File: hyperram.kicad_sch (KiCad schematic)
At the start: 7 parts, among them U11 S27KL0641DABHI023

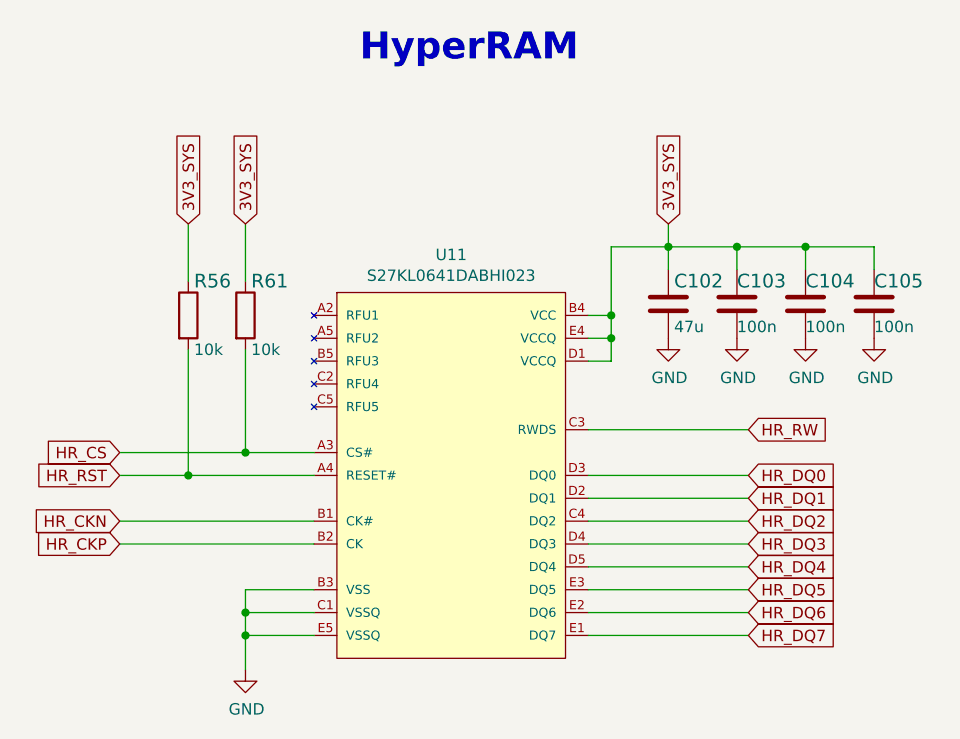
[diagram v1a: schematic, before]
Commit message: Readability improvements
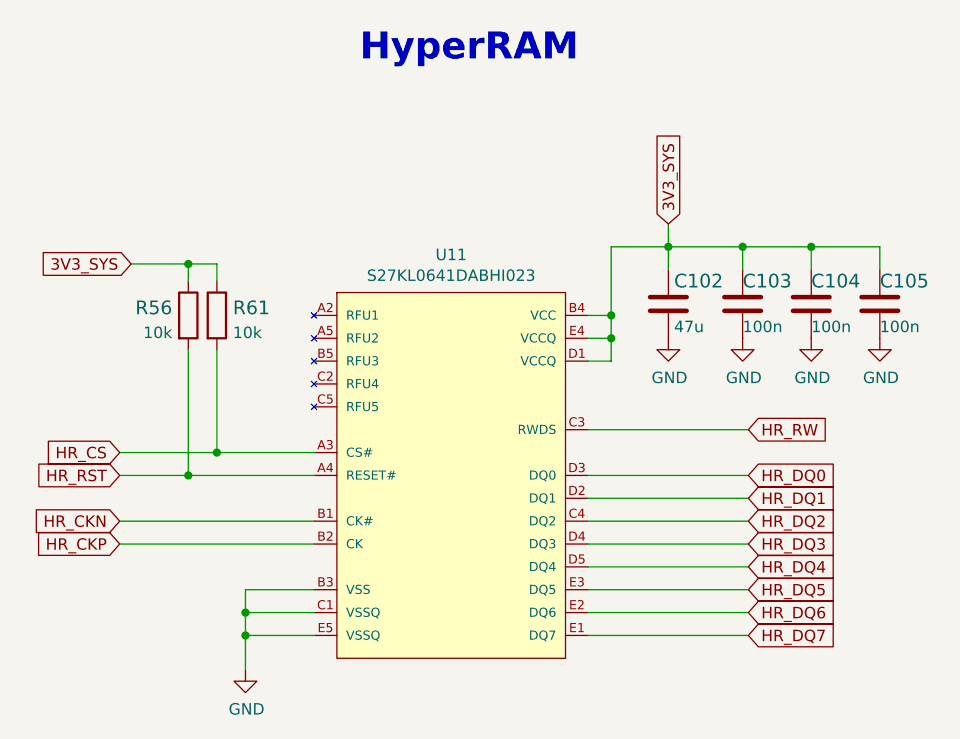
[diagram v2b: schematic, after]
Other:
- moved on the sheet: C103, C104, C105, R61

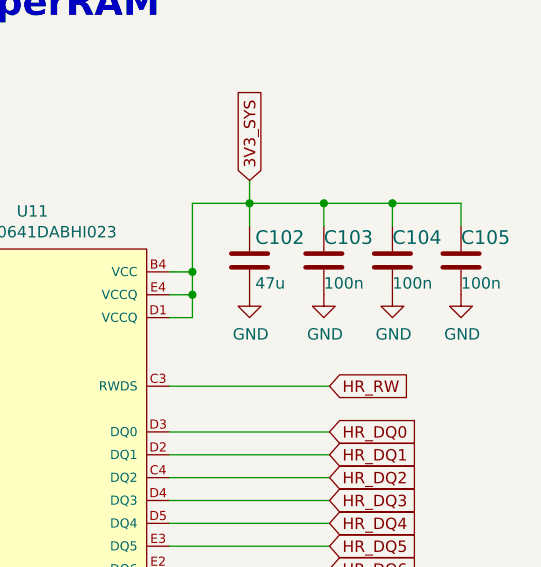
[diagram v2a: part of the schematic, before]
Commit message: Implement all review fixes, route control signals from FMC to FPGA
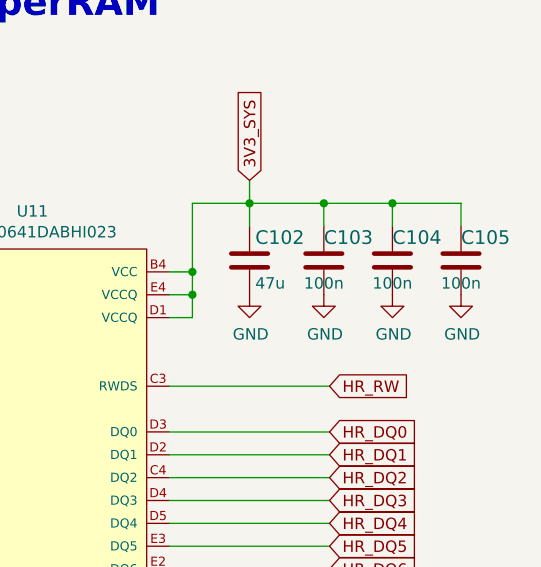
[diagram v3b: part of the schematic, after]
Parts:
- C103, C104, C105: value C_100n_0402_6V3 -> C_100n_0402; footprint data-center-dram-tester-footprints:0402-cap -> antmicro-footprints:0402-cap; symbol data-center-dram-tester:C_100n_0402_6V3 -> antmicroCapacitors0402:C_100n_0402; MPN 0402X104K6R3CT -> GRM155R61H104KE14D; Manufacturer Walsin -> Murata
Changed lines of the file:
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@@
     (pin "2")
   )
-  (symbol (lib_id "data-center-dram-tester:C_100n_0402_6V3") (at 236.22 131.445 0) (unit 1)
+  (symbol (lib_id "antmicroCapacitors0402:C_100n_0402") (at 236.22 131.445 0) (unit 1)
     (in_bom yes) (on_board yes)
     (property "Reference" "C104" (id 0) (at 236.22 128.905 0)
       (effects (font (size 1.524 1.524)) (justify left))
     )
-    (property "Value" "C_100n_0402_6V3" (id 1) (at 236.22 135.255 0)
+    (property "Value" "C_100n_0402" (id 1) (at 236.22 135.255 0)
       (effects (font (size 1.524 1.524)) hide)
     )
-    (property "Footprint" "data-center-dram-tester-footprints:0402-cap" (id 2) (at 241.3 126.365 0)
+    (property "Footprint" "antmicro-footprints:0402-cap" (id 2) (at 241.3 126.365 0)
       (effects (font (size 1.524 1.524)) (justify left) hide)
     )
@@
       (effects (font (size 1.27 1.27)) hide)
     )
-    (property "Manufacturer" "Walsin" (id 4) (at 241.3 121.285 0)
+    (property "Manufacturer" "Murata" (id 4) (at 241.3 121.285 0)
       (effects (font (size 1.524 1.524)) (justify left) hide)
     )
-    (property "MPN" "0402X104K6R3CT" (id 5) (at 241.3 123.825 0)
+    (property "MPN" "GRM155R61H104KE14D" (id 5) (at 241.3 123.825 0)
       (effects (font (size 1.524 1.524)) (justify left) hide)
     )
-    (property "Val" "100n" (id 6) (at 236.22 133.985 0)
-      (effects (font (size 1.27 1.27)) (justify left))
-    )
+    (property "Val" "100n" (id 6) (at 236.22 133.985 0))
     (pin "1")
     (pin "2")
@@
     (pin "1")
   )
-  (symbol (lib_id "data-center-dram-tester:C_100n_0402_6V3") (at 228.6 131.445 0) (unit 1)
+  (symbol (lib_id "antmicroCapacitors0402:C_100n_0402") (at 228.6 131.445 0) (unit 1)
     (in_bom yes) (on_board yes)
     (property "Reference" "C103" (id 0) (at 228.6 128.905 0)
       (effects (font (size 1.524 1.524)) (justify left))
     )
-    (property "Value" "C_100n_0402_6V3" (id 1) (at 228.6 135.255 0)
+    (property "Value" "C_100n_0402" (id 1) (at 228.6 135.255 0)
       (effects (font (size 1.524 1.524)) hide)
     )
-    (property "Footprint" "data-center-dram-tester-footprints:0402-cap" (id 2) (at 233.68 126.365 0)
+    (property "Footprint" "antmicro-footprints:0402-cap" (id 2) (at 233.68 126.365 0)
       (effects (font (size 1.524 1.524)) (justify left) hide)
     )
@@
       (effects (font (size 1.27 1.27)) hide)
     )
-    (property "Manufacturer" "Walsin" (id 4) (at 233.68 121.285 0)
+    (property "Manufacturer" "Murata" (id 4) (at 233.68 121.285 0)
       (effects (font (size 1.524 1.524)) (justify left) hide)
     )
-    (property "MPN" "0402X104K6R3CT" (id 5) (at 233.68 123.825 0)
+    (property "MPN" "GRM155R61H104KE14D" (id 5) (at 233.68 123.825 0)
       (effects (font (size 1.524 1.524)) (justify left) hide)
     )
-    (property "Val" "100n" (id 6) (at 228.6 133.985 0)
-      (effects (font (size 1.27 1.27)) (justify left))
-    )
+    (property "Val" "100n" (id 6) (at 228.6 133.985 0))
     (pin "1")
     (pin "2")
@@
     (pin "1")
   )
-  (symbol (lib_id "data-center-dram-tester:C_100n_0402_6V3") (at 243.84 131.445 0) (unit 1)
+  (symbol (lib_id "antmicroCapacitors0402:C_100n_0402") (at 243.84 131.445 0) (unit 1)
     (in_bom yes) (on_board yes)
     (property "Reference" "C105" (id 0) (at 243.84 128.905 0)
       (effects (font (size 1.524 1.524)) (justify left))
     )
-    (property "Value" "C_100n_0402_6V3" (id 1) (at 243.84 135.255 0)
+    (property "Value" "C_100n_0402" (id 1) (at 243.84 135.255 0)
       (effects (font (size 1.524 1.524)) hide)
     )
-    (property "Footprint" "data-center-dram-tester-footprints:0402-cap" (id 2) (at 248.92 126.365 0)
+    (property "Footprint" "antmicro-footprints:0402-cap" (id 2) (at 248.92 126.365 0)
       (effects (font (size 1.524 1.524)) (justify left) hide)
     )
@@
       (effects (font (size 1.27 1.27)) hide)
     )
-    (property "Manufacturer" "Walsin" (id 4) (at 248.92 121.285 0)
+    (property "Manufacturer" "Murata" (id 4) (at 248.92 121.285 0)
       (effects (font (size 1.524 1.524)) (justify left) hide)
     )
-    (property "MPN" "0402X104K6R3CT" (id 5) (at 248.92 123.825 0)
+    (property "MPN" "GRM155R61H104KE14D" (id 5) (at 248.92 123.825 0)
       (effects (font (size 1.524 1.524)) (justify left) hide)
     )
-    (property "Val" "100n" (id 6) (at 243.84 133.985 0)
-      (effects (font (size 1.27 1.27)) (justify left))
-    )
+    (property "Val" "100n" (id 6) (at 243.84 133.985 0))
     (pin "1")
     (pin "2")
